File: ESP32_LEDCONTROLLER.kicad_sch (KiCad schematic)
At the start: 20 parts, among them J1 ST-04, J2 ST-00, J3 ST-01, J4 ST-02, J5 ST-03, U1 LM2576HVT-5, U2 ESP32_NODEMCU, U3 SN74LV4T125

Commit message: v0.1 of the LED Controller has been completed.
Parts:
- removed U2: ESP32_NODEMCU, Esp32NodeMCU:MODULE_ESP32_NODEMCU, symbol ESP32_NODEMCU:ESP32_NODEMCU
- added U2: ESP32-DEVKIT-V1, MODULE_ESP32_DEVKIT_V1, symbol ESP32-DEVKIT-V1:ESP32-DEVKIT-V1
- U3: footprint (none) -> Package_DIP:DIP-14_W7.62mm
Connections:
- net GND: now also U2.2 (GND), U2.29 (GND)
- net VCC: now also U2.30 (VIN)
- net at U3.2: now also U2.24 (D26)
- net at U3.5: now also U2.25 (D27)
- net at R4.1: now also U2.8 (D5)
- net at R3.1: now also U2.5 (D4)
- net at U3.12: now also U2.22 (D33)
- net at U3.9: now also U2.23 (D25)
- net at R2.1: now also U2.4 (D2)
- net at R1.1: now also U2.3 (D15)
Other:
- moved on the sheet: J2, J3, J4, J5, R1, R2, R3, R4, R5, R6, R7, R8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

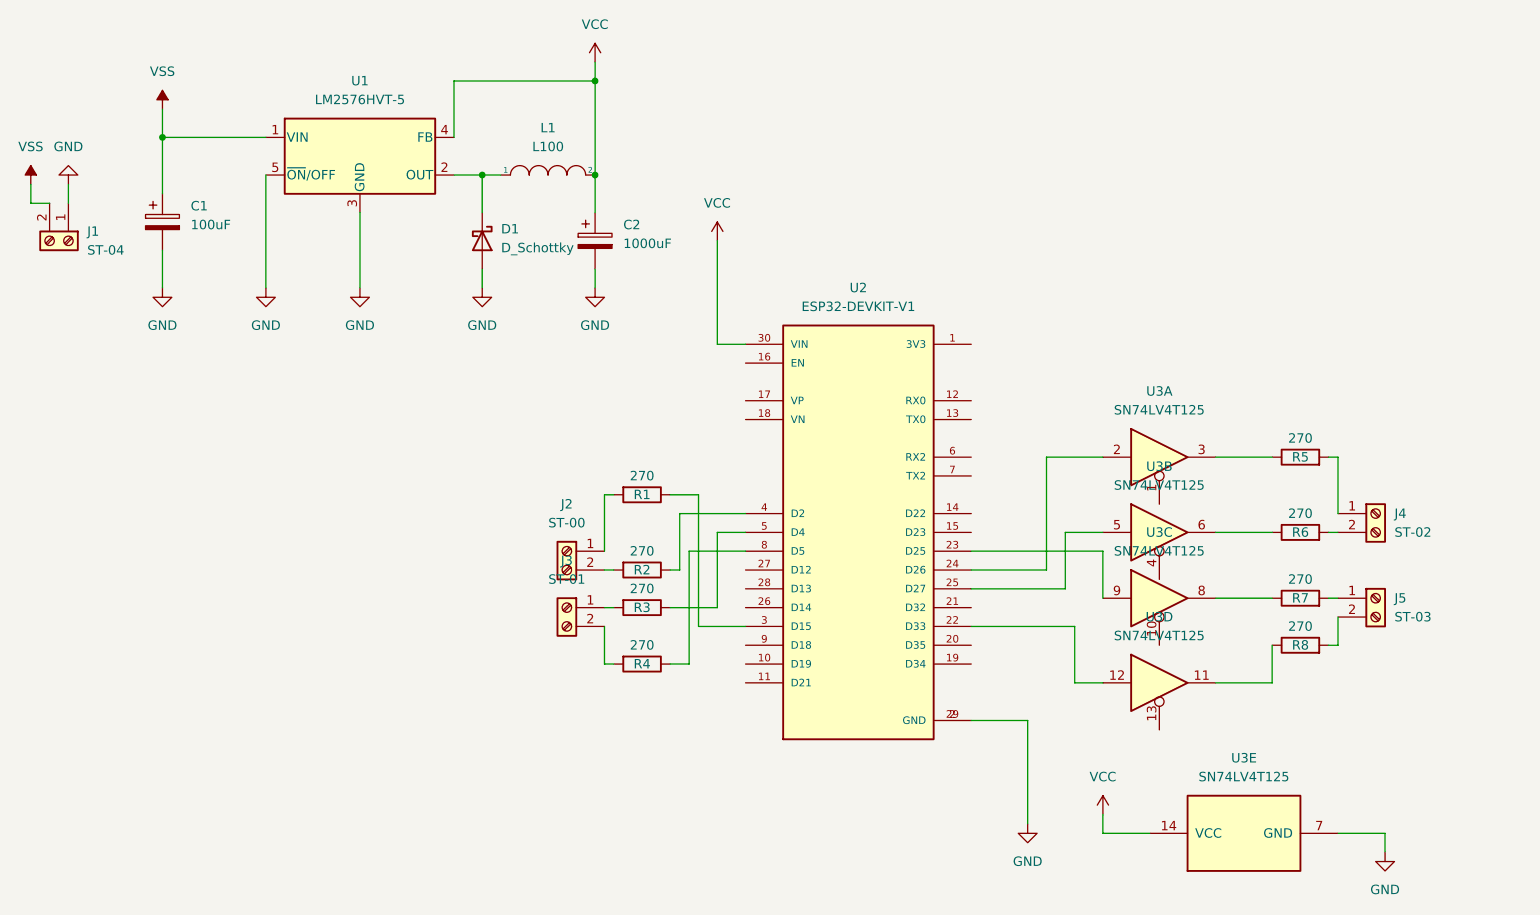
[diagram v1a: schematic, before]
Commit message: Refactor by dropping level shifter & changing board layout
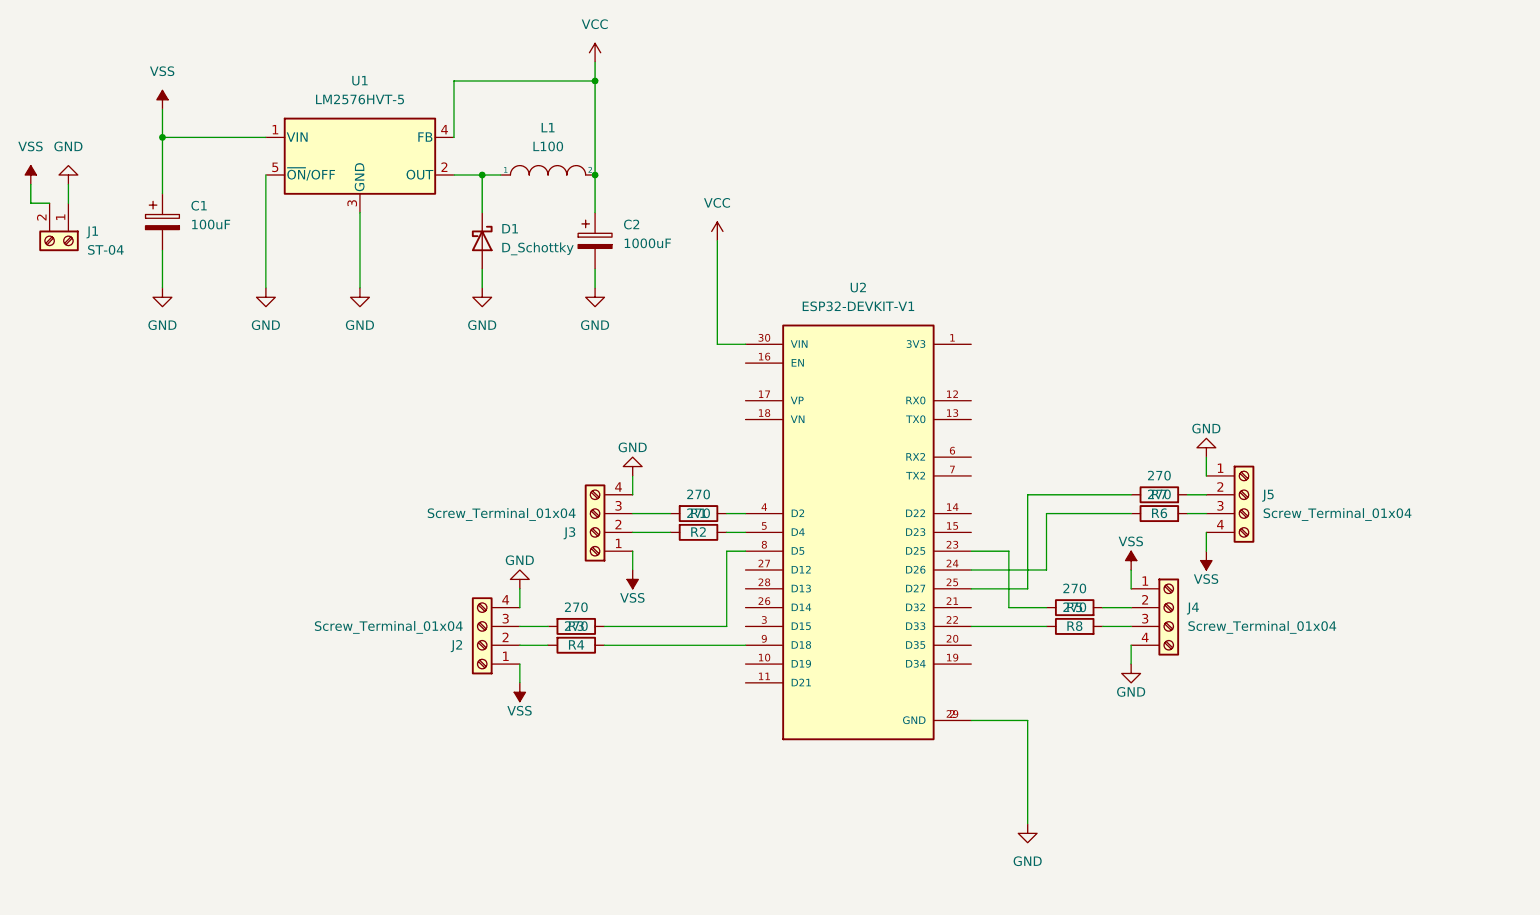
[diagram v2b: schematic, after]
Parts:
- removed J2: ST-00, TerminalBlock:TerminalBlock_bornier-2_P5.08mm, symbol Connector:Screw_Terminal_01x02
- removed J3: ST-01, TerminalBlock:TerminalBlock_bornier-2_P5.08mm, symbol Connector:Screw_Terminal_01x02
- removed J4: ST-02, TerminalBlock:TerminalBlock_bornier-2_P5.08mm, symbol Connector:Screw_Terminal_01x02
- removed J5: ST-03, TerminalBlock:TerminalBlock_bornier-2_P5.08mm, symbol Connector:Screw_Terminal_01x02
- removed U3: SN74LV4T125, Package_DIP:DIP-14_W7.62mm, symbol 74xx:SN74LV4T125
- added J2, J3, J4, J5: Screw_Terminal_01x04, TerminalBlock_4Ucon:TerminalBlock_4Ucon_1x04_P3.50mm_Horizontal, symbol Connector:Screw_Terminal_01x04
- U2: footprint MODULE_ESP32_DEVKIT_V1 -> ESP32-Devkitv1:MODULE_ESP32_DEVKIT_V1
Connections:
- net GND: now also J2.4 (Pin_4), J3.4 (Pin_4), J4.4 (Pin_4), J5.1 (Pin_1)
- net VSS: now also J2.1 (Pin_1), J3.1 (Pin_1), J4.1 (Pin_1), J5.4 (Pin_4)
- net at U2.24 (D26): now also R6.1
- net at R5.1: now also U2.23 (D25)
- net at R1.2: now also J3.3 (Pin_3)
- net at R2.2: now also J3.2 (Pin_2)
- net at U2.22 (D33): now also R8.1
- net at U2.25 (D27): now also R7.1
- net at U2.3 (D15): no longer R1.1
- net at U2.4 (D2): now also R1.1; no longer R2.1
- net at U2.5 (D4): now also R2.1; no longer R3.1
- net at U2.8 (D5): now also R3.1; no longer R4.1
- net at U2.9 (D18): now also R4.1
- net at R8.2: now also J4.3 (Pin_3)
- net at R5.2: now also J4.2 (Pin_2)
- net at R3.2: now also J2.3 (Pin_3)
- net at R4.2: now also J2.2 (Pin_2)
- net at R6.2: now also J5.3 (Pin_3)
- net at R7.2: now also J5.2 (Pin_2)
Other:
- moved on the sheet: R1, R2, R3, R4, R5, R6, R7, R8

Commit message: graphics & shitposting
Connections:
- net GND: now also J5.4 (Pin_4); no longer J5.1 (Pin_1)
- net VSS: now also J5.1 (Pin_1); no longer J5.4 (Pin_4)
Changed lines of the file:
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@@
+    (stroke (width 0) (type default) (color 0 0 0 0))
+  )
+  (wire (pts (xy 111.76 39.37) (xy 111.76 52.07))
+    (stroke (width 0) (type default) (color 0 0 0 0))
+  )
+  (wire (pts (xy 101.6 115.57) (xy 105.41 115.57))
+    (stroke (width 0) (type default) (color 0 0 0 0))
+  )
+  (wire (pts (xy 116.84 105.41) (xy 116.84 102.87))
+    (stroke (width 0) (type default) (color 0 0 0 0))
+  )
+  (wire (pts (xy 170.18 95.25) (xy 184.15 95.25))
+    (stroke (width 0) (type default) (color 0 0 0 0))
+  )
+  (wire (pts (xy 129.54 97.79) (xy 132.08 97.79))
+    (stroke (width 0) (type default) (color 0 0 0 0))
+  )
+  (wire (pts (xy 111.76 52.07) (xy 111.76 57.15))
+    (stroke (width 0) (type default) (color 0 0 0 0))
+  )
+  (wire (pts (xy 128.27 74.93) (xy 132.08 74.93))
+    (stroke (width 0) (type default) (color 0 0 0 0))
+  )
+  (wire (pts (xy 162.56 113.03) (xy 172.72 113.03))
+    (stroke (width 0) (type default) (color 0 0 0 0))
+  )
+  (wire (pts (xy 40.64 53.34) (xy 40.64 55.88))
+    (stroke (width 0) (type default) (color 0 0 0 0))
+  )
+  (wire (pts (xy 116.84 95.25) (xy 116.84 92.71))
+    (stroke (width 0) (type default) (color 0 0 0 0))
+  )
+  (wire (pts (xy 170.18 107.95) (xy 170.18 95.25))
+    (stroke (width 0) (type default) (color 0 0 0 0))
+  )
+  (wire (pts (xy 101.6 110.49) (xy 101.6 107.95))
+    (stroke (width 0) (type default) (color 0 0 0 0))
+  )
+  (wire (pts (xy 132.08 115.57) (xy 113.03 115.57))
+    (stroke (width 0) (type default) (color 0 0 0 0))
+  )
+  (wire (pts (xy 101.6 113.03) (xy 105.41 113.03))
+    (stroke (width 0) (type default) (color 0 0 0 0))
+  )
+  (wire (pts (xy 184.15 105.41) (xy 184.15 107.95))
+    (stroke (width 0) (type default) (color 0 0 0 0))
+  )
+  (wire (pts (xy 111.76 36.83) (xy 111.76 39.37))
+    (stroke (width 0) (type default) (color 0 0 0 0))
+  )
+  (wire (pts (xy 96.52 52.07) (xy 96.52 57.15))
+    (stroke (width 0) (type default) (color 0 0 0 0))
+  )
+  (wire (pts (xy 184.15 115.57) (xy 184.15 118.11))
+    (stroke (width 0) (type default) (color 0 0 0 0))
+  )
+  (wire (pts (xy 96.52 64.77) (xy 96.52 67.31))
+    (stroke (width 0) (type default) (color 0 0 0 0))
+  )
+  (wire (pts (xy 53.34 62.23) (xy 53.34 67.31))
+    (stroke (width 0) (type default) (color 0 0 0 0))
+  )
+  (wire (pts (xy 172.72 97.79) (xy 184.15 97.79))
+    (stroke (width 0) (type default) (color 0 0 0 0))
+  )
+  (wire (pts (xy 172.72 105.41) (xy 172.72 97.79))
+    (stroke (width 0) (type default) (color 0 0 0 0))
+  )
+  (wire (pts (xy 162.56 102.87) (xy 167.64 102.87))
+    (stroke (width 0) (type default) (color 0 0 0 0))
+  )
+  (wire (pts (xy 180.34 110.49) (xy 184.15 110.49))
+    (stroke (width 0) (type default) (color 0 0 0 0))
+  )
+  (wire (pts (xy 35.56 53.34) (xy 35.56 55.88))
+    (stroke (width 0) (type default) (color 0 0 0 0))
+  )
+  (wire (pts (xy 113.03 113.03) (xy 129.54 113.03))
+    (stroke (width 0) (type default) (color 0 0 0 0))
+  )
+  (wire (pts (xy 167.64 110.49) (xy 172.72 110.49))
+    (stroke (width 0) (type default) (color 0 0 0 0))
+  )
+  (wire (pts (xy 53.34 43.18) (xy 53.34 46.99))
+    (stroke (width 0) (type default) (color 0 0 0 0))
+  )
+  (wire (pts (xy 132.08 102.87) (xy 129.54 102.87))
+    (stroke (width 0) (type default) (color 0 0 0 0))
+  )
+  (wire (pts (xy 191.77 95.25) (xy 194.31 95.25))
+    (stroke (width 0) (type default) (color 0 0 0 0))
+  )
+  (wire (pts (xy 191.77 97.79) (xy 194.31 97.79))
     (stroke (width 0) (type default) (color 0 0 0 0))
   )
@@
     (stroke (width 0) (type default) (color 0 0 0 0))
   )
-  (wire (pts (xy 111.76 39.37) (xy 111.76 52.07))
-    (stroke (width 0) (type default) (color 0 0 0 0))
-  )
-  (wire (pts (xy 101.6 115.57) (xy 105.41 115.57))
-    (stroke (width 0) (type default) (color 0 0 0 0))
-  )
-  (wire (pts (xy 116.84 105.41) (xy 116.84 102.87))
-    (stroke (width 0) (type default) (color 0 0 0 0))
-  )
-  (wire (pts (xy 170.18 95.25) (xy 184.15 95.25))
-    (stroke (width 0) (type default) (color 0 0 0 0))
-  )
-  (wire (pts (xy 129.54 97.79) (xy 132.08 97.79))
-    (stroke (width 0) (type default) (color 0 0 0 0))
-  )
-  (wire (pts (xy 111.76 52.07) (xy 111.76 57.15))
-    (stroke (width 0) (type default) (color 0 0 0 0))
-  )
-  (wire (pts (xy 128.27 74.93) (xy 132.08 74.93))
-    (stroke (width 0) (type default) (color 0 0 0 0))
-  )
-  (wire (pts (xy 162.56 113.03) (xy 172.72 113.03))
-    (stroke (width 0) (type default) (color 0 0 0 0))
-  )
-  (wire (pts (xy 40.64 53.34) (xy 40.64 55.88))
-    (stroke (width 0) (type default) (color 0 0 0 0))
-  )
-  (wire (pts (xy 116.84 95.25) (xy 116.84 92.71))
-    (stroke (width 0) (type default) (color 0 0 0 0))
-  )
-  (wire (pts (xy 170.18 107.95) (xy 170.18 95.25))
-    (stroke (width 0) (type default) (color 0 0 0 0))
-  )
-  (wire (pts (xy 101.6 110.49) (xy 101.6 107.95))
-    (stroke (width 0) (type default) (color 0 0 0 0))
-  )
-  (wire (pts (xy 132.08 115.57) (xy 113.03 115.57))
-    (stroke (width 0) (type default) (color 0 0 0 0))
-  )
-  (wire (pts (xy 101.6 113.03) (xy 105.41 113.03))
-    (stroke (width 0) (type default) (color 0 0 0 0))
-  )
-  (wire (pts (xy 184.15 105.41) (xy 184.15 107.95))
-    (stroke (width 0) (type default) (color 0 0 0 0))
-  )
-  (wire (pts (xy 111.76 36.83) (xy 111.76 39.37))
-    (stroke (width 0) (type default) (color 0 0 0 0))
-  )
-  (wire (pts (xy 96.52 52.07) (xy 96.52 57.15))
-    (stroke (width 0) (type default) (color 0 0 0 0))
-  )
-  (wire (pts (xy 184.15 115.57) (xy 184.15 118.11))
-    (stroke (width 0) (type default) (color 0 0 0 0))
-  )
-  (wire (pts (xy 96.52 64.77) (xy 96.52 67.31))
-    (stroke (width 0) (type default) (color 0 0 0 0))
-  )
-  (wire (pts (xy 53.34 62.23) (xy 53.34 67.31))
-    (stroke (width 0) (type default) (color 0 0 0 0))
-  )
-  (wire (pts (xy 172.72 97.79) (xy 184.15 97.79))
-    (stroke (width 0) (type default) (color 0 0 0 0))
-  )
-  (wire (pts (xy 172.72 105.41) (xy 172.72 97.79))
-    (stroke (width 0) (type default) (color 0 0 0 0))
-  )
-  (wire (pts (xy 162.56 102.87) (xy 167.64 102.87))
-    (stroke (width 0) (type default) (color 0 0 0 0))
-  )
-  (wire (pts (xy 180.34 110.49) (xy 184.15 110.49))
-    (stroke (width 0) (type default) (color 0 0 0 0))
-  )
-  (wire (pts (xy 35.56 53.34) (xy 35.56 55.88))
-    (stroke (width 0) (type default) (color 0 0 0 0))
-  )
-  (wire (pts (xy 113.03 113.03) (xy 129.54 113.03))
-    (stroke (width 0) (type default) (color 0 0 0 0))
-  )
-  (wire (pts (xy 167.64 110.49) (xy 172.72 110.49))
-    (stroke (width 0) (type default) (color 0 0 0 0))
-  )
-  (wire (pts (xy 53.34 43.18) (xy 53.34 46.99))
-    (stroke (width 0) (type default) (color 0 0 0 0))
-  )
-  (wire (pts (xy 132.08 102.87) (xy 129.54 102.87))
-    (stroke (width 0) (type default) (color 0 0 0 0))
-  )
-  (wire (pts (xy 191.77 95.25) (xy 194.31 95.25))
-    (stroke (width 0) (type default) (color 0 0 0 0))
-  )
-  (wire (pts (xy 191.77 97.79) (xy 194.31 97.79))
-    (stroke (width 0) (type default) (color 0 0 0 0))
-  )
   (wire (pts (xy 170.18 139.7) (xy 170.18 125.73))
     (stroke (width 0) (type default) (color 0 0 0 0))
@@
     (stroke (width 0) (type default) (color 0 0 0 0))
   )
+  (wire (pts (xy 194.31 100.33) (xy 194.31 102.87))
+    (stroke (width 0) (type default) (color 0 0 0 0))
+  )
   (wire (pts (xy 101.6 120.65) (xy 101.6 118.11))
     (stroke (width 0) (type default) (color 0 0 0 0))
@@
   )
   (wire (pts (xy 162.56 107.95) (xy 170.18 107.95))
-    (stroke (width 0) (type default) (color 0 0 0 0))
-  )
-  (wire (pts (xy 194.31 100.33) (xy 194.31 102.87))
     (stroke (width 0) (type default) (color 0 0 0 0))
   )
@@
     (pin "1")
   )
-  (symbol (lib_id "power:VSS") (at 194.31 102.87 180) (unit 1)
-    (in_bom yes) (on_board yes)
-    (property "Reference" "#PWR018" (id 0) (at 194.31 99.06 0)
-      (effects (font (size 1.27 1.27)) hide)
-    )
-    (property "Value" "VSS" (id 1) (at 194.31 106.68 0))
-    (property "Footprint" "" (id 2) (at 194.31 102.87 0)
-      (effects (font (size 1.27 1.27)) hide)
-    )
-    (property "Datasheet" "" (id 3) (at 194.31 102.87 0)
+  (symbol (lib_id "power:VSS") (at 194.31 90.17 0) (mirror y) (unit 1)
+    (in_bom yes) (on_board yes)
+    (property "Reference" "#PWR018" (id 0) (at 194.31 93.98 0)
+      (effects (font (size 1.27 1.27)) hide)
+    )
+    (property "Value" "VSS" (id 1) (at 194.31 86.36 0))
+    (property "Footprint" "" (id 2) (at 194.31 90.17 0)
+      (effects (font (size 1.27 1.27)) hide)
+    )
+    (property "Datasheet" "" (id 3) (at 194.31 90.17 0)
       (effects (font (size 1.27 1.27)) hide)
     )
@@
     (pin "2")
   )
-  (symbol (lib_id "power:GND") (at 194.31 90.17 180) (unit 1)
-    (in_bom yes) (on_board yes)
-    (property "Reference" "#PWR019" (id 0) (at 194.31 83.82 0)
-      (effects (font (size 1.27 1.27)) hide)
-    )
-    (property "Value" "GND" (id 1) (at 194.31 86.36 0))
-    (property "Footprint" "" (id 2) (at 194.31 90.17 0)
-      (effects (font (size 1.27 1.27)) hide)
-    )
-    (property "Datasheet" "" (id 3) (at 194.31 90.17 0)
-      (effects (font (size 1.27 1.27)) hide)
-    )
+  (symbol (lib_id "power:GND") (at 194.31 102.87 0) (unit 1)
+    (in_bom yes) (on_board yes)
+    (property "Reference" "#PWR019" (id 0) (at 194.31 109.22 0)
+      (effects (font (size 1.27 1.27)) hide)
+    )
+    (property "Value" "GND" (id 1) (at 194.31 106.68 0))
+    (property "Footprint" "" (id 2) (at 194.31 102.87 0)
+      (effects (font (size 1.27 1.27)) hide)
+    )
+    (property "Datasheet" "" (id 3) (at 194.31 102.87 0)
+      (effects (font (size 1.27 1.27)) hide)
+    )
